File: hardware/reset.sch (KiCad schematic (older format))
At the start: 9 parts, among them SW5 Reset, U15 MAX705, U16 74HC175

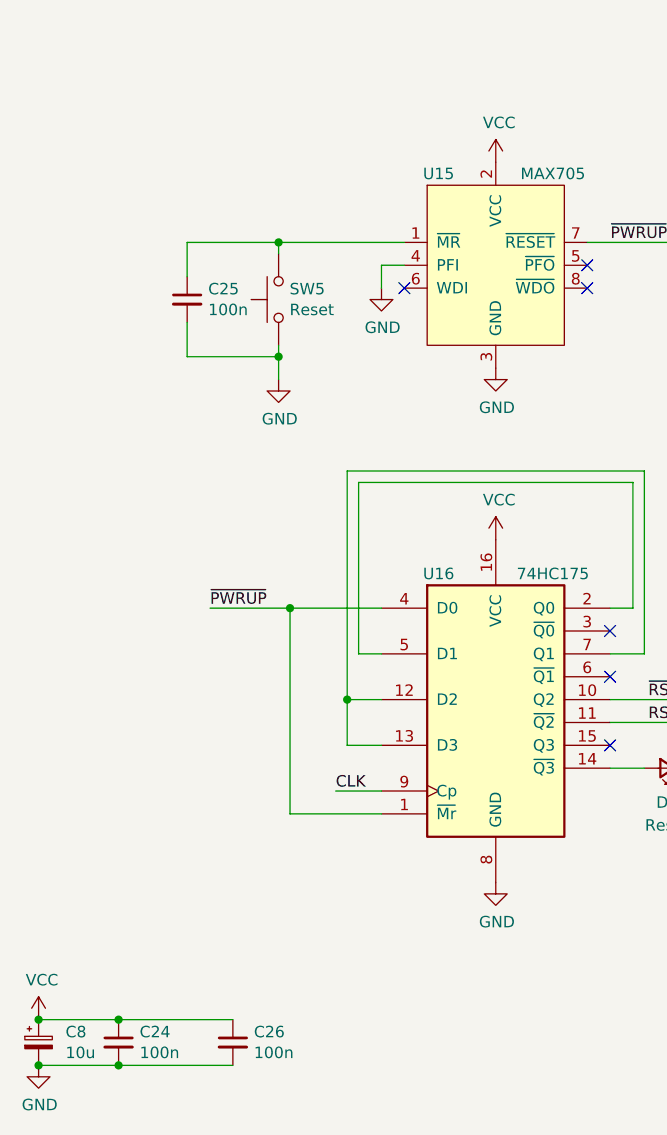
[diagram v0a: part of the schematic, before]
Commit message: Re-number parts
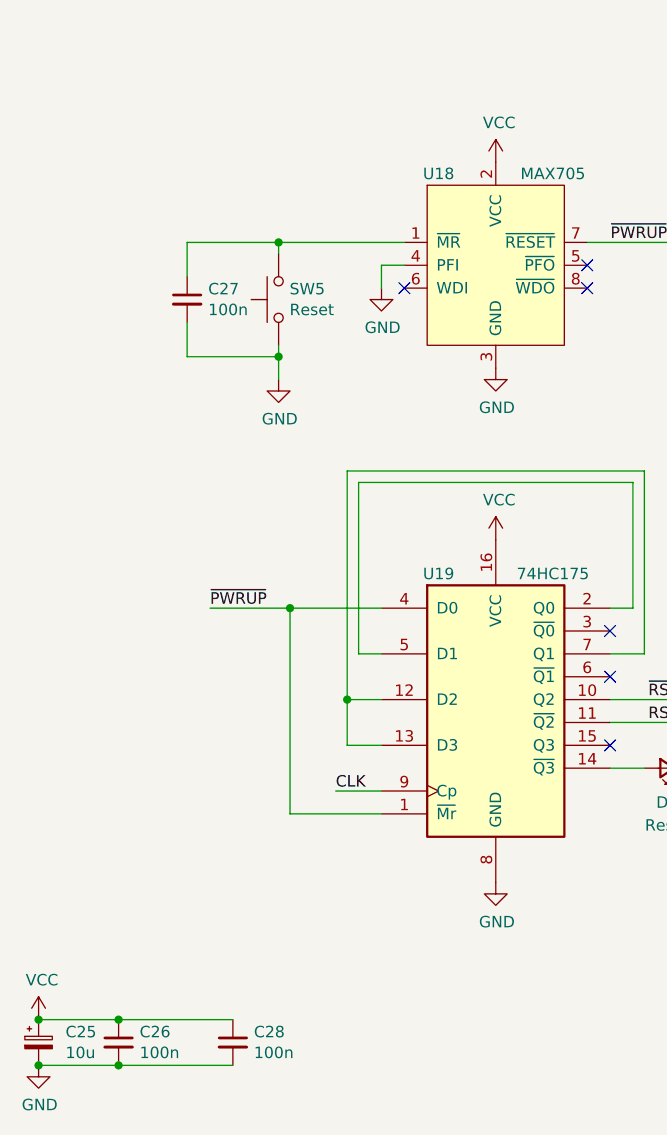
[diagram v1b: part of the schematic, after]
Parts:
- renumbered C8 to C25, C24 to C26, C25 to C27, C26 to C28, U15 to U18, U16 to U19
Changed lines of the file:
@@
 ~RST
 $Comp
-L 65C816:MAX705 U15
+L 65C816:MAX705 U18
 U 1 1 61967767
 P 5750 3500
-F 0 "U15" H 5500 3900 50  0000 C CNN
+F 0 "U18" H 5500 3900 50  0000 C CNN
 F 1 "MAX705" H 6000 3900 50  0000 C CNN
 F 2 "" H 5650 3900 50  0001 C CNN
@@
 $EndComp
 $Comp
-L power:VCC #PWR064
+L power:VCC #PWR080
 U 1 1 619687FB
 P 5750 3050
-F 0 "#PWR064" H 5750 2900 50  0001 C CNN
+F 0 "#PWR080" H 5750 2900 50  0001 C CNN
 F 1 "VCC" H 5765 3223 50  0000 C CNN
 F 2 "" H 5750 3050 50  0001 C CNN
@@
 $EndComp
 $Comp
-L power:GND #PWR065
+L power:GND #PWR081
 U 1 1 61969010
 P 5750 3950
-F 0 "#PWR065" H 5750 3700 50  0001 C CNN
+F 0 "#PWR081" H 5750 3700 50  0001 C CNN
 F 1 "GND" H 5755 3777 50  0000 C CNN
 F 2 "" H 5750 3950 50  0001 C CNN
@@
 	5350 3400 4800 3400
 $Comp
-L power:GND #PWR066
+L power:GND #PWR078
 U 1 1 6196A930
 P 4800 4000
-F 0 "#PWR066" H 4800 3750 50  0001 C CNN
+F 0 "#PWR078" H 4800 3750 50  0001 C CNN
 F 1 "GND" H 4805 3827 50  0000 C CNN
 F 2 "" H 4800 4000 50  0001 C CNN
@@
 CLK
 $Comp
-L Device:C_Small C24
+L Device:C_Small C26
 U 1 1 619750B8
 P 4100 6900
-F 0 "C24" H 4192 6946 50  0000 L CNN
+F 0 "C26" H 4192 6946 50  0000 L CNN
 F 1 "100n" H 4192 6855 50  0000 L CNN
 F 2 "" H 4100 6900 50  0001 C CNN
@@
 $EndComp
 $Comp
-L Device:C_Small C26
+L Device:C_Small C28
 U 1 1 61975352
 P 4600 6900
-F 0 "C26" H 4692 6946 50  0000 L CNN
+F 0 "C28" H 4692 6946 50  0000 L CNN
 F 1 "100n" H 4692 6855 50  0000 L CNN
 F 2 "" H 4600 6900 50  0001 C CNN
@@
 	4100 7000 4600 7000
 $Comp
-L power:VCC #PWR069
+L power:VCC #PWR076
 U 1 1 6197B488
 P 3750 6800
-F 0 "#PWR069" H 3750 6650 50  0001 C CNN
+F 0 "#PWR076" H 3750 6650 50  0001 C CNN
 F 1 "VCC" H 3765 6973 50  0000 C CNN
 F 2 "" H 3750 6800 50  0001 C CNN
@@
 $EndComp
 $Comp
-L power:GND #PWR070
+L power:GND #PWR077
 U 1 1 6197B8F7
 P 3750 7000
-F 0 "#PWR070" H 3750 6750 50  0001 C CNN
+F 0 "#PWR077" H 3750 6750 50  0001 C CNN
 F 1 "GND" H 3755 6827 50  0000 C CNN
 F 2 "" H 3750 7000 50  0001 C CNN
@@
 $EndComp
 $Comp
-L power:GND #PWR071
+L power:GND #PWR084
 U 1 1 6199B290
 P 6700 6000
-F 0 "#PWR071" H 6700 5750 50  0001 C CNN
+F 0 "#PWR084" H 6700 5750 50  0001 C CNN
 F 1 "GND" H 6705 5827 50  0000 C CNN
 F 2 "" H 6700 6000 50  0001 C CNN
@@
 	6700 5700 6700 5750
 $Comp
-L Device:C_Small C25
+L Device:C_Small C27
 U 1 1 6199E70D
 P 4400 3650
-F 0 "C25" H 4492 3696 50  0000 L CNN
+F 0 "C27" H 4492 3696 50  0000 L CNN
 F 1 "100n" H 4492 3605 50  0000 L CNN
 F 2 "" H 4400 3650 50  0001 C CNN
@@
 	4800 3900 4800 3850
 $Comp
-L power:GND #PWR0107
+L power:GND #PWR079
 U 1 1 61A1E3A3
 P 5250 3600
-F 0 "#PWR0107" H 5250 3350 50  0001 C CNN
+F 0 "#PWR079" H 5250 3350 50  0001 C CNN
 F 1 "GND" H 5255 3427 50  0000 C CNN
 F 2 "" H 5250 3600 50  0001 C CNN
@@
 P 3750 6900
 AR Path="/61A44297" Ref="C?"  Part="1"
-AR Path="/61B33617/61A44297" Ref="C8"  Part="1"
-F 0 "C8" H 3868 6946 50  0000 L CNN
+AR Path="/61B33617/61A44297" Ref="C25"  Part="1"
+F 0 "C25" H 3868 6946 50  0000 L CNN
 F 1 "10u" H 3868 6855 50  0000 L CNN
 F 2 "" H 3788 6750 50  0001 C CNN
@@
 Connection ~ 3750 6800
 $Comp
-L 74xx:74LS175 U16
+L 74xx:74LS175 U19
 U 1 1 619D9E86
 P 5750 5400
-F 0 "U16" H 5500 5950 50  0000 C CNN
+F 0 "U19" H 5500 5950 50  0000 C CNN
 F 1 "74HC175" H 6000 5950 50  0000 C CNN
 F 2 "" H 5750 5400 50  0001 C CNN
@@
 NoConn ~ 6250 5100
 $Comp
-L power:VCC #PWR08
+L power:VCC #PWR082
 U 1 1 619EE9D1
 P 5750 4700
-F 0 "#PWR08" H 5750 4550 50  0001 C CNN
+F 0 "#PWR082" H 5750 4550 50  0001 C CNN
 F 1 "VCC" H 5765 4873 50  0000 C CNN
 F 2 "" H 5750 4700 50  0001 C CNN
@@
 $EndComp
 $Comp
-L power:GND #PWR09
+L power:GND #PWR083
 U 1 1 619EEF3B
 P 5750 6200
-F 0 "#PWR09" H 5750 5950 50  0001 C CNN
+F 0 "#PWR083" H 5750 5950 50  0001 C CNN
 F 1 "GND" H 5755 6027 50  0000 C CNN
 F 2 "" H 5750 6200 50  0001 C CNN

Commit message: Updates for Episode 12
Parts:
- added D4: PWRUP, symbol Device:LED_Small
- added R12: 1k, symbol Device:R_Small
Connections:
- net VCC: now also D4.2 (A)
- net ~PWRUP: now also R12.2
- new net: D4.1 (K), R12.1
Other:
- moved on the sheet: C25, C26, C27, C28, D3, R11, SW5, U18, U19
